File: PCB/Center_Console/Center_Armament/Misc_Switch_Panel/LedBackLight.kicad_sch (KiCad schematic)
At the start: 18 parts

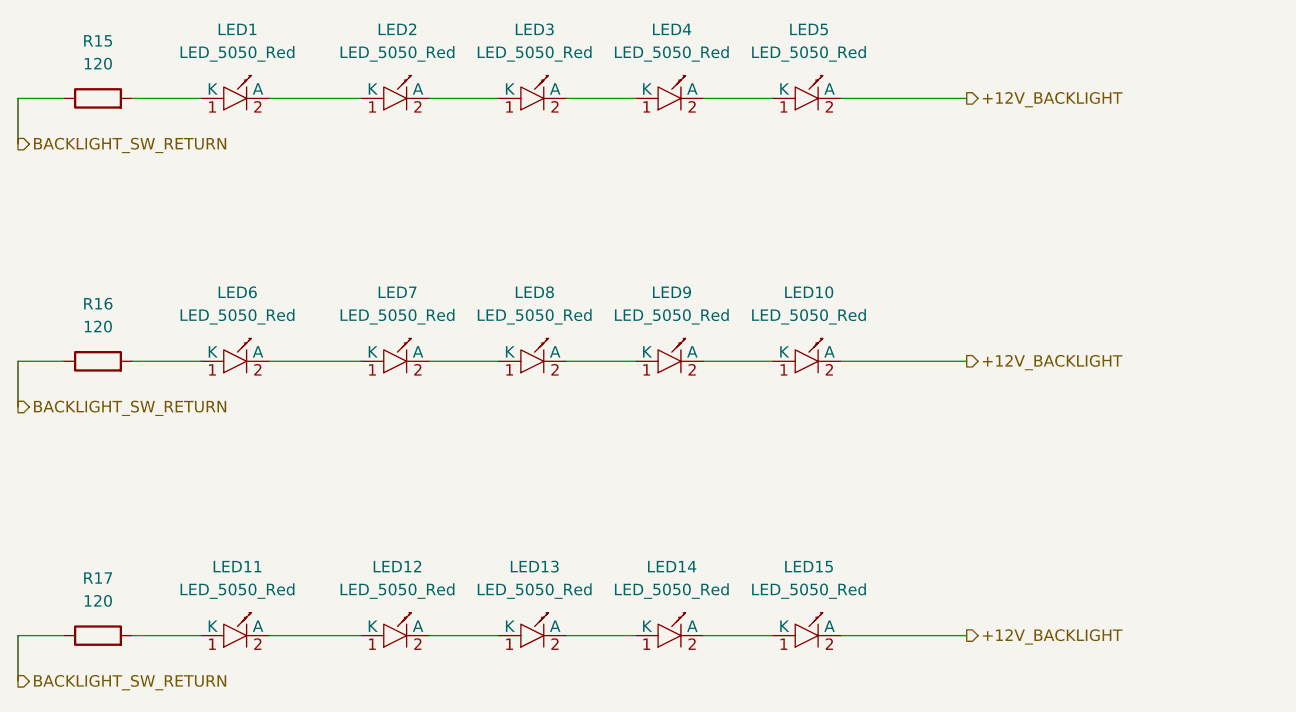
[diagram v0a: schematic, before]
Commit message: Fix LED_5050_Red symbol polarity: K=pin1, A=pin2
Symbol body was mirrored vs standard Device:LED convention — pin 1 was
labelled A and pin 2 K. Flipped triangle/bar to point left and swapped
pin names so K=1 (left) and A=2 (right), matching the generic KiCad LED
symbol.

Physical LED verified: notched/chamfered corner is the ANODE. Footprint
pad positions unchanged — pad2 (left, where the silkscreen marker sits)
is now correctly the anode. Updated kicad.md to document this.

Also includes Misc_Switch_Panel schematic edits from current KiCad session.
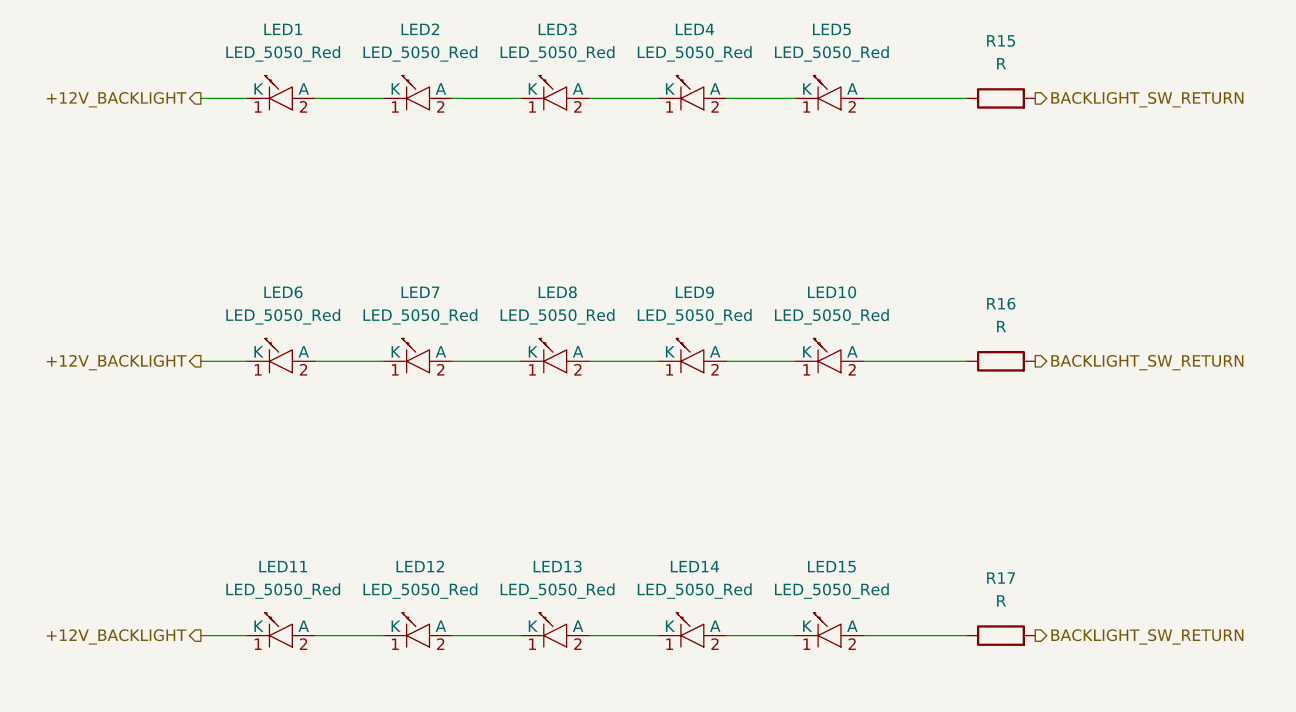
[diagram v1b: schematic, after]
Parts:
- R15, R16, R17: value 120 -> R
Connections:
- net +12V_BACKLIGHT: now also LED1.1 (K), LED11.1 (K), LED6.1 (K); no longer LED10.2 (A), LED15.2 (A), LED5.2 (A)
- net BACKLIGHT_SW_RETURN: now also R15.2, R16.2, R17.2; no longer R15.1, R16.1, R17.1
- new net: LED15.2 (A), R17.1
- new net: LED10.2 (A), R16.1
- new net: LED5.2 (A), R15.1
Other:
- moved on the sheet: LED1, LED10, LED11, LED12, LED13, LED14, LED15, LED2, LED3, LED4, LED5, LED6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

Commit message: Scaffold AWRS_Panel and Armament_MCU KiCad projects
- AWRS_Panel: breakout board scaffold (sym-lib-table, fp-lib-table,
  jlcpcb-standard.kicad_dru, .kicad_pro, .kicad_sch)
- Armament_MCU: MCU board scaffold (same set of files)
- Add controller stub docs: AWRS_Panel.md and Armament_Panel.md
- Update Center_Armament.md harness section: J1→AWRS_Panel and
  J2→Misc_Switch_Panel documented as two distinct connectors with
  full pinouts; J2_LED Mini-Fit Jr added
- Misc_Switch_Panel: KiCad reformatted files on project open
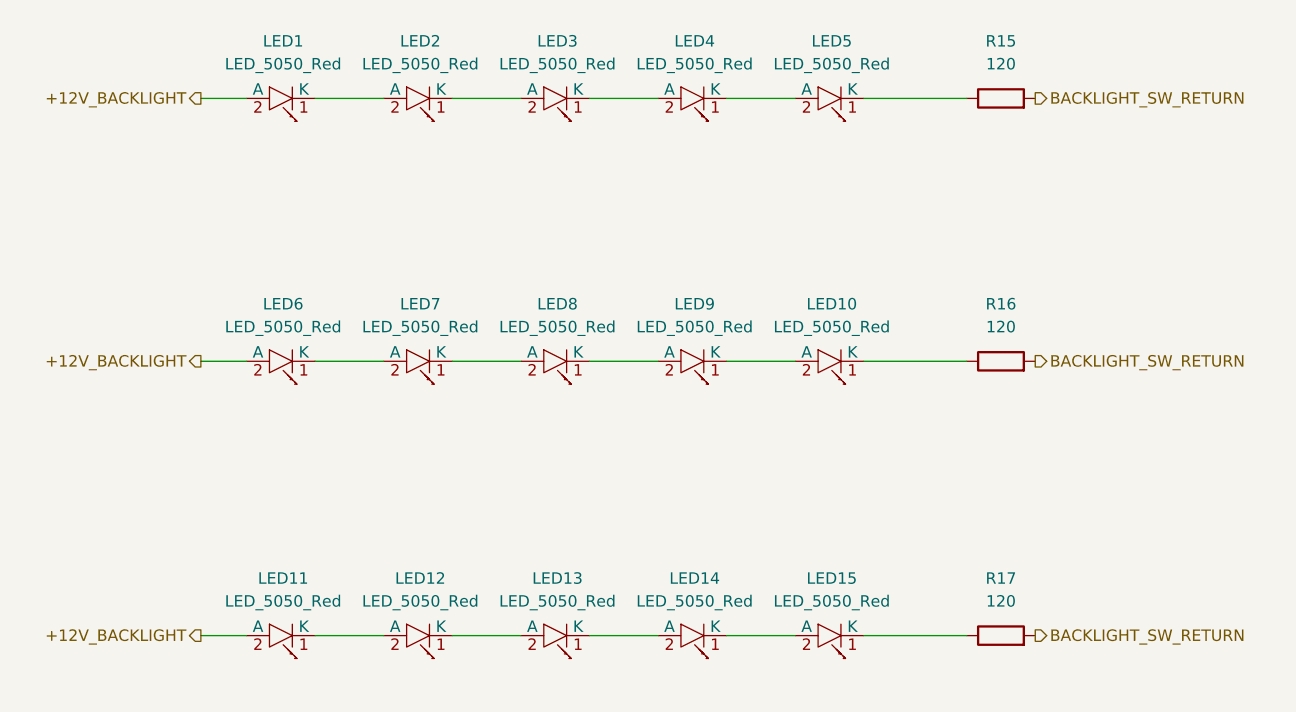
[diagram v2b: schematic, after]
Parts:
- R15, R16, R17: value R -> 120
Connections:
- net +12V_BACKLIGHT: now also LED1.2 (A), LED11.2 (A), LED6.2 (A); no longer LED1.1 (K), LED11.1 (K), LED6.1 (K)
- net at LED14.1 (K): now also LED15.2 (A); no longer LED13.2 (A)
- net at LED14.2 (A): now also LED13.1 (K); no longer LED15.1 (K)
- net at R17.1: now also LED15.1 (K); no longer LED15.2 (A)
- net at R16.1: now also LED10.1 (K); no longer LED10.2 (A)
- net at R15.1: now also LED5.1 (K); no longer LED5.2 (A)
- net at LED9.2 (A): now also LED8.1 (K); no longer LED10.1 (K)
- net at LED12.2 (A): now also LED11.1 (K); no longer LED13.1 (K)
- net at LED2.1 (K): now also LED3.2 (A); no longer LED1.2 (A)
- net at LED2.2 (A): now also LED1.1 (K); no longer LED3.1 (K)
- net at LED4.1 (K): now also LED5.2 (A); no longer LED3.2 (A)
- net at LED4.2 (A): now also LED3.1 (K); no longer LED5.1 (K)
- net at LED7.1 (K): now also LED8.2 (A); no longer LED6.2 (A)
- net at LED12.1 (K): now also LED13.2 (A); no longer LED11.2 (A)
- net at LED9.1 (K): now also LED10.2 (A); no longer LED8.2 (A)
- net at LED7.2 (A): now also LED6.1 (K); no longer LED8.1 (K)
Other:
- moved on the sheet: LED1, LED10, LED11, LED12, LED13, LED14, LED15, LED2, LED3, LED4, LED5, LED6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
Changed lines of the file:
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@@
 	(symbol
 		(lib_id "OpenSkyhawk:LED_5050_Red")
-		(at 100.33 119.38 0)
+		(at 100.33 119.38 180)
 		(unit 1)
 		(body_style 1)
@@
 		(fields_autoplaced yes)
 		(property "Reference" "LED14"
-			(at 100.584 111.76 0)
+			(at 100.584 113.03 0)
 			(show_name no)
 			(do_not_autoplace no)
@@
 		)
 		(property "Value" "LED_5050_Red"
-			(at 100.584 114.3 0)
+			(at 100.584 115.57 0)
 			(show_name no)
 			(do_not_autoplace no)
@@
 	(symbol
 		(lib_id "OpenSkyhawk:LED_5050_Red")
-		(at 115.57 119.38 0)
+		(at 115.57 119.38 180)
 		(unit 1)
 		(body_style 1)
@@
 		(fields_autoplaced yes)
 		(property "Reference" "LED15"
-			(at 115.824 111.76 0)
+			(at 115.824 113.03 0)
 			(show_name no)
 			(do_not_autoplace no)
@@
 		)
 		(property "Value" "LED_5050_Red"
-			(at 115.824 114.3 0)
+			(at 115.824 115.57 0)
 			(show_name no)
 			(do_not_autoplace no)
@@
 			)
 		)
-		(property "Value" "R"
+		(property "Value" "120"
 			(at 134.62 115.57 90)
 			(show_name no)
@@
 			)
 		)
-		(property "Value" "R"
+		(property "Value" "120"
 			(at 134.62 85.09 90)
 			(show_name no)
@@
 			)
 		)
-		(property "Value" "R"
+		(property "Value" "120"
 			(at 134.62 55.88 90)
 			(show_name no)
@@
 	(symbol
 		(lib_id "OpenSkyhawk:LED_5050_Red")
-		(at 115.57 88.9 0)
+		(at 115.57 88.9 180)
 		(unit 1)
 		(body_style 1)
@@
 		(fields_autoplaced yes)
 		(property "Reference" "LED10"
-			(at 115.824 81.28 0)
+			(at 115.824 82.55 0)
 			(show_name no)
 			(do_not_autoplace no)
@@
 		)
 		(property "Value" "LED_5050_Red"
-			(at 115.824 83.82 0)
+			(at 115.824 85.09 0)
 			(show_name no)
 			(do_not_autoplace no)
@@
 	(symbol
 		(lib_id "OpenSkyhawk:LED_5050_Red")
-		(at 85.09 119.38 0)
+		(at 85.09 119.38 180)
 		(unit 1)
 		(body_style 1)
@@
 		(fields_autoplaced yes)
 		(property "Reference" "LED13"
-			(at 85.344 111.76 0)
+			(at 85.344 113.03 0)
 			(show_name no)
 			(do_not_autoplace no)
@@
 		)
 		(property "Value" "LED_5050_Red"
-			(at 85.344 114.3 0)
+			(at 85.344 115.57 0)
 			(show_name no)
 			(do_not_autoplace no)
@@
 	(symbol
 		(lib_id "OpenSkyhawk:LED_5050_Red")
-		(at 69.85 59.69 0)
+		(at 69.85 59.69 180)
 		(unit 1)
 		(body_style 1)
@@
 		(fields_autoplaced yes)
 		(property "Reference" "LED2"
-			(at 70.104 52.07 0)
+			(at 70.104 53.34 0)
 			(show_name no)
 			(do_not_autoplace no)
@@
 		)
 		(property "Value" "LED_5050_Red"
-			(at 70.104 54.61 0)
+			(at 70.104 55.88 0)
 			(show_name no)
 			(do_not_autoplace no)
@@
 	(symbol
 		(lib_id "OpenSkyhawk:LED_5050_Red")
-		(at 100.33 59.69 0)
+		(at 100.33 59.69 180)
 		(unit 1)
 		(body_style 1)
@@
 		(fields_autoplaced yes)
 		(property "Reference" "LED4"
-			(at 100.584 52.07 0)
+			(at 100.584 53.34 0)
 			(show_name no)
 			(do_not_autoplace no)
@@
 		)
 		(property "Value" "LED_5050_Red"
-			(at 100.584 54.61 0)
+			(at 100.584 55.88 0)
 			(show_name no)
 			(do_not_autoplace no)
@@
 	(symbol
 		(lib_id "OpenSkyhawk:LED_5050_Red")
-		(at 54.61 88.9 0)
+		(at 54.61 88.9 180)
 		(unit 1)
 		(body_style 1)
@@
 		(fields_autoplaced yes)
 		(property "Reference" "LED6"
-			(at 54.864 81.28 0)
+			(at 54.864 82.55 0)
 			(show_name no)
 			(do_not_autoplace no)
@@
 		)
 		(property "Value" "LED_5050_Red"
-			(at 54.864 83.82 0)
+			(at 54.864 85.09 0)
 			(show_name no)
 			(do_not_autoplace no)
@@
 	(symbol
 		(lib_id "OpenSkyhawk:LED_5050_Red")
-		(at 115.57 59.69 0)
+		(at 115.57 59.69 180)
 		(unit 1)
 		(body_style 1)
@@
 		(fields_autoplaced yes)
 		(property "Reference" "LED5"
-			(at 115.824 52.07 0)
+			(at 115.824 53.34 0)
 			(show_name no)
 			(do_not_autoplace no)
@@
 		)
 		(property "Value" "LED_5050_Red"
-			(at 115.824 54.61 0)
+			(at 115.824 55.88 0)
 			(show_name no)
 			(do_not_autoplace no)
@@
 	(symbol
 		(lib_id "OpenSkyhawk:LED_5050_Red")
-		(at 69.85 119.38 0)
+		(at 69.85 119.38 180)
 		(unit 1)
 		(body_style 1)
@@
 		(fields_autoplaced yes)
 		(property "Reference" "LED12"
-			(at 70.104 111.76 0)
+			(at 70.104 113.03 0)
 			(show_name no)
 			(do_not_autoplace no)
@@
 		)
 		(property "Value" "LED_5050_Red"
-			(at 70.104 114.3 0)
+			(at 70.104 115.57 0)
 			(show_name no)
 			(do_not_autoplace no)
@@
 	(symbol
 		(lib_id "OpenSkyhawk:LED_5050_Red")
-		(at 54.61 119.38 0)
+		(at 54.61 119.38 180)
 		(unit 1)
 		(body_style 1)
@@
 		(fields_autoplaced yes)
 		(property "Reference" "LED11"
-			(at 54.864 111.76 0)
+			(at 54.864 113.03 0)
 			(show_name no)
 			(do_not_autoplace no)
@@
 		)
 		(property "Value" "LED_5050_Red"
-			(at 54.864 114.3 0)
+			(at 54.864 115.57 0)
 			(show_name no)
 			(do_not_autoplace no)
@@
 	(symbol
 		(lib_id "OpenSkyhawk:LED_5050_Red")
-		(at 100.33 88.9 0)
+		(at 100.33 88.9 180)
 		(unit 1)
 		(body_style 1)
@@
 		(fields_autoplaced yes)
 		(property "Reference" "LED9"
-			(at 100.584 81.28 0)
+			(at 100.584 82.55 0)
 			(show_name no)
 			(do_not_autoplace no)
@@
 		)
 		(property "Value" "LED_5050_Red"
-			(at 100.584 83.82 0)
+			(at 100.584 85.09 0)
 			(show_name no)
 			(do_not_autoplace no)
@@
 	(symbol
 		(lib_id "OpenSkyhawk:LED_5050_Red")
-		(at 69.85 88.9 0)
+		(at 69.85 88.9 180)
 		(unit 1)
 		(body_style 1)
@@
 		(fields_autoplaced yes)
 		(property "Reference" "LED7"
-			(at 70.104 81.28 0)
+			(at 70.104 82.55 0)
 			(show_name no)
 			(do_not_autoplace no)
@@
 		)
 		(property "Value" "LED_5050_Red"
-			(at 70.104 83.82 0)
+			(at 70.104 85.09 0)
 			(show_name no)
 			(do_not_autoplace no)
@@
 	(symbol
 		(lib_id "OpenSkyhawk:LED_5050_Red")
-		(at 85.09 88.9 0)
+		(at 85.09 88.9 180)
 		(unit 1)
 		(body_style 1)
@@
 		(fields_autoplaced yes)
 		(property "Reference" "LED8"
-			(at 85.344 81.28 0)
+			(at 85.344 82.55 0)
 			(show_name no)
 			(do_not_autoplace no)
@@
 		)
 		(property "Value" "LED_5050_Red"
-			(at 85.344 83.82 0)
+			(at 85.344 85.09 0)
 			(show_name no)
 			(do_not_autoplace no)
@@
 	(symbol
 		(lib_id "OpenSkyhawk:LED_5050_Red")
-		(at 85.09 59.69 0)
+		(at 85.09 59.69 180)
 		(unit 1)
 		(body_style 1)
@@
 		(fields_autoplaced yes)
 		(property "Reference" "LED3"
-			(at 85.344 52.07 0)
+			(at 85.344 53.34 0)
 			(show_name no)
 			(do_not_autoplace no)
@@
 		)
 		(property "Value" "LED_5050_Red"
-			(at 85.344 54.61 0)
+			(at 85.344 55.88 0)
 			(show_name no)
 			(do_not_autoplace no)
@@
 	(symbol
 		(lib_id "OpenSkyhawk:LED_5050_Red")
-		(at 54.61 59.69 0)
+		(at 54.61 59.69 180)
 		(unit 1)
 		(body_style 1)
@@
 		(fields_autoplaced yes)
 		(property "Reference" "LED1"
-			(at 54.864 52.07 0)
+			(at 54.864 53.34 0)
 			(show_name no)
 			(do_not_autoplace no)
@@
 		)
 		(property "Value" "LED_5050_Red"
-			(at 54.864 54.61 0)
-			(show_name no)
-			(do_not_autoplace no)
+			(at 54.864 55.88 0)
+			(show_name no)
+			(do_not_autoplace no)
